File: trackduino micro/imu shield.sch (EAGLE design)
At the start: 11 parts, among them U1 LSM9DS1

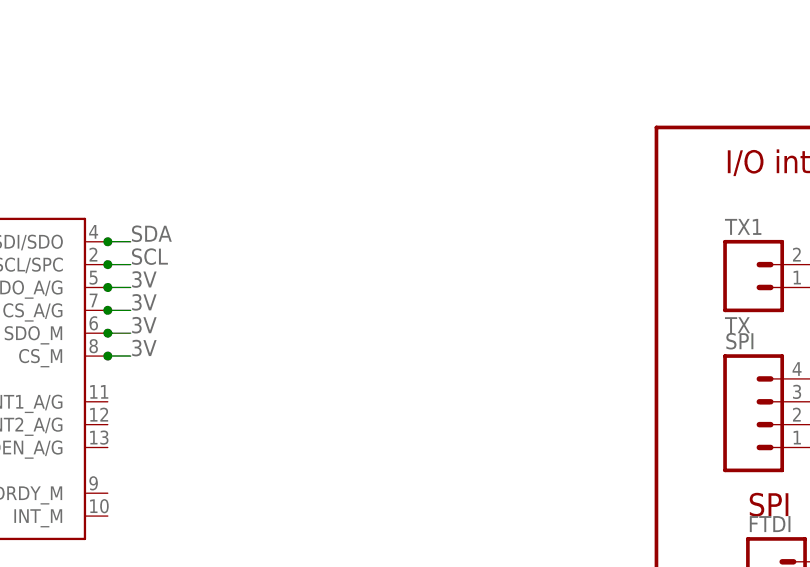
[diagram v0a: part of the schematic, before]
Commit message: added reg to imu shield
added 3v regulator to IMU shield
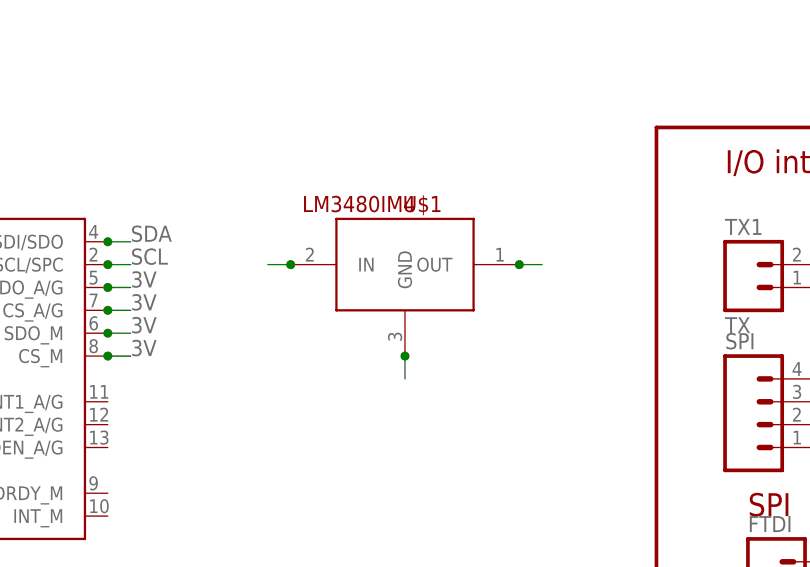
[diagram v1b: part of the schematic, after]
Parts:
- added U$1: LM3480IM4, SparkFun-PowerIC:LM3480IM4
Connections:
- net GND: now also U$1.GND
- net VCC: now also U$1.IN
- net VDD: now also U$1.OUT
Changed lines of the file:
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@@
 <part name="C4" library="SparkFun-Passives" deviceset="CAP" device="0805" value="10nf"/>
 <part name="C5" library="SparkFun-Passives" deviceset="CAP" device="0805" value=".1uf"/>
+<part name="U$1" library="SparkFun-PowerIC" deviceset="LM3480IM4" device=""/>
 </parts>
 <sheets>
@@
 <instance part="C4" gate="G$1" x="71.12" y="91.44"/>
 <instance part="C5" gate="G$1" x="78.74" y="91.44"/>
+<instance part="U$1" gate="G$1" x="154.94" y="93.98"/>
 </instances>
 <busses>
@@
 <label x="83.82" y="66.04" size="1.778" layer="95"/>
 </segment>
+<segment>
+<pinref part="U$1" gate="G$1" pin="GND"/>
+<wire x1="154.94" y1="83.82" x2="154.94" y2="81.28" width="0.1524" layer="91"/>
+<junction x="154.94" y="83.82"/>
+</segment>
 </net>
 <net name="VCC" class="0">
@@
 <junction x="203.2" y="55.88"/>
 <junction x="208.28" y="55.88"/>
+</segment>
+<segment>
+<pinref part="U$1" gate="G$1" pin="IN"/>
+<wire x1="142.24" y1="93.98" x2="139.7" y2="93.98" width="0.1524" layer="91"/>
+<junction x="142.24" y="93.98"/>
 </segment>
 </net>
@@
 <junction x="91.44" y="93.98"/>
 </segment>
-</net>
+<segment>
+<pinref part="U$1" gate="G$1" pin="OUT"/>
+<wire x1="167.64" y1="93.98" x2="170.18" y2="93.98" width="0.1524" layer="91"/>
+<junction x="167.64" y="93.98"/>
+</segment>
+</net>

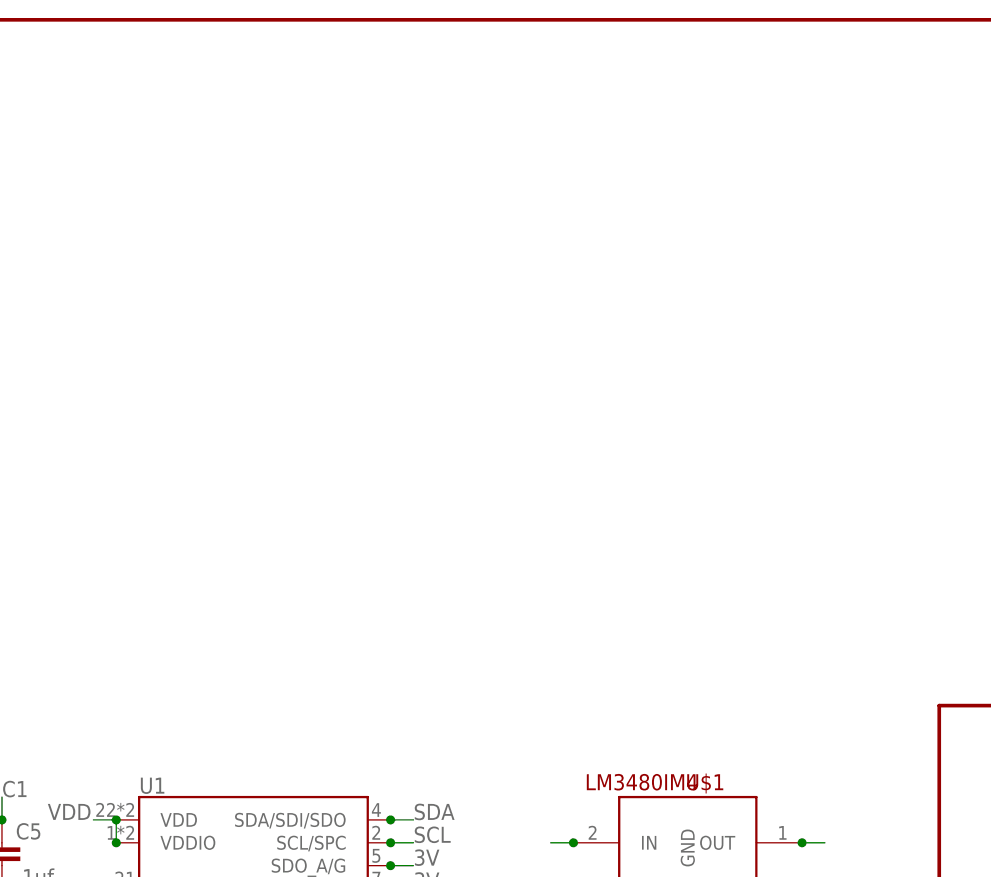
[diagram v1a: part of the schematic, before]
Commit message: Shield Updates
added sd storage shield, added fetid chip to programming shield. Moved
test boards to correct folder.
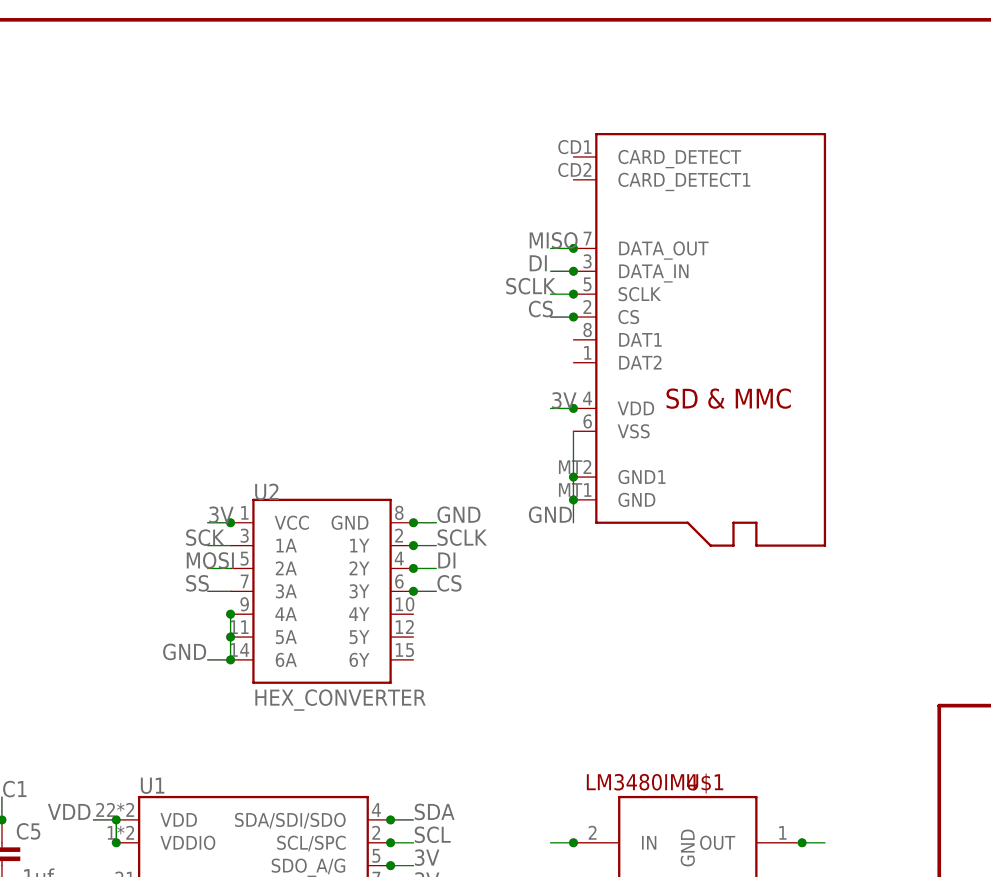
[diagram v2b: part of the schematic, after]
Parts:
- added U$2: MICROSD, adafruit:MICROSD
- added U2: HEX_CONVERTER, SparkFun-DigitalIC:HEX_CONVERTER
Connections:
- new net CS: U$2.CS, U2.3Y
- new net DI: U$2.DATA_IN, U2.2Y
- new net SCLK: U$2.SCLK, U2.1Y
- net 3V: now also U$2.VDD, U2.VCC
- net GND: now also U$2.GND, U$2.GND1, U$2.VSS, U2.4A, U2.5A, U2.6A, U2.GND
- net MISO: now also U$2.DATA_OUT
- net MOSI: now also U2.2A
- net SCK: now also U2.1A
- net SS: now also U2.3A
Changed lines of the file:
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@@
 <layer number="230" name="230bmp" color="7" fill="1" visible="yes" active="yes"/>
 <layer number="231" name="231bmp" color="7" fill="1" visible="yes" active="yes"/>
+<layer number="232" name="Eagle3D_PG2" color="7" fill="1" visible="no" active="no"/>
+<layer number="233" name="Eagle3D_PG3" color="7" fill="1" visible="no" active="no"/>
 <layer number="248" name="Housing" color="7" fill="1" visible="yes" active="yes"/>
 <layer number="249" name="Edge" color="7" fill="1" visible="yes" active="yes"/>
@@
 <part name="C5" library="SparkFun-Passives" deviceset="CAP" device="0805" value=".1uf"/>
 <part name="U$1" library="SparkFun-PowerIC" deviceset="LM3480IM4" device=""/>
+<part name="U2" library="SparkFun-DigitalIC" deviceset="HEX_CONVERTER" device=""/>
+<part name="U$2" library="adafruit" deviceset="MICROSD" device=""/>
 </parts>
 <sheets>
@@
 <instance part="C5" gate="G$1" x="78.74" y="91.44"/>
 <instance part="U$1" gate="G$1" x="154.94" y="93.98"/>
+<instance part="U2" gate="G$1" x="114.3" y="121.92"/>
+<instance part="U$2" gate="G$1" x="160.02" y="152.4"/>
 </instances>
 <busses>
@@
 <junction x="154.94" y="83.82"/>
 </segment>
+<segment>
+<pinref part="U$2" gate="G$1" pin="VSS"/>
+<wire x1="142.24" y1="139.7" x2="142.24" y2="134.62" width="0.1524" layer="91"/>
+<label x="137.16" y="129.54" size="1.778" layer="95"/>
+<pinref part="U$2" gate="G$1" pin="GND"/>
+<junction x="142.24" y="132.08"/>
+<wire x1="142.24" y1="134.62" x2="142.24" y2="132.08" width="0.1524" layer="91"/>
+<wire x1="142.24" y1="132.08" x2="142.24" y2="129.54" width="0.1524" layer="91"/>
+<pinref part="U$2" gate="G$1" pin="GND1"/>
+<junction x="142.24" y="134.62"/>
+</segment>
+<segment>
+<pinref part="U2" gate="G$1" pin="GND"/>
+<wire x1="124.46" y1="129.54" x2="127" y2="129.54" width="0.1524" layer="91"/>
+<label x="127" y="129.54" size="1.778" layer="95"/>
+<junction x="124.46" y="129.54"/>
+</segment>
+<segment>
+<pinref part="U2" gate="G$1" pin="5A"/>
+<pinref part="U2" gate="G$1" pin="6A"/>
+<wire x1="104.14" y1="116.84" x2="104.14" y2="114.3" width="0.1524" layer="91"/>
+<wire x1="104.14" y1="114.3" x2="101.6" y2="114.3" width="0.1524" layer="91"/>
+<label x="96.52" y="114.3" size="1.778" layer="95"/>
+<junction x="104.14" y="116.84"/>
+<junction x="104.14" y="114.3"/>
+<pinref part="U2" gate="G$1" pin="4A"/>
+<wire x1="104.14" y1="119.38" x2="104.14" y2="116.84" width="0.1524" layer="91"/>
+<junction x="104.14" y="119.38"/>
+</segment>
 </net>
 <net name="VCC" class="0">
@@
 <junction x="200.66" y="76.2"/>
 </segment>
+<segment>
+<pinref part="U$2" gate="G$1" pin="DATA_OUT"/>
+<wire x1="142.24" y1="160.02" x2="139.7" y2="160.02" width="0.1524" layer="91"/>
+<label x="137.16" y="160.02" size="1.778" layer="95"/>
+<junction x="142.24" y="160.02"/>
+</segment>
 </net>
 <net name="MOSI" class="0">
@@
 <junction x="200.66" y="78.74"/>
 </segment>
+<segment>
+<pinref part="U2" gate="G$1" pin="2A"/>
+<wire x1="104.14" y1="124.46" x2="101.6" y2="124.46" width="0.1524" layer="91"/>
+<label x="99.06" y="124.46" size="1.778" layer="95"/>
+</segment>
 </net>
 <net name="SCK" class="0">
@@
 <junction x="200.66" y="73.66"/>
 </segment>
+<segment>
+<pinref part="U2" gate="G$1" pin="1A"/>
+<wire x1="104.14" y1="127" x2="101.6" y2="127" width="0.1524" layer="91"/>
+<label x="99.06" y="127" size="1.778" layer="95"/>
+</segment>
 </net>
 <net name="SS" class="0">
@@
 <label x="203.2" y="81.28" size="1.778" layer="95"/>
 <junction x="200.66" y="81.28"/>
+</segment>
+<segment>
+<pinref part="U2" gate="G$1" pin="3A"/>
+<wire x1="104.14" y1="121.92" x2="101.6" y2="121.92" width="0.1524" layer="91"/>
+<label x="99.06" y="121.92" size="1.778" layer="95"/>
 </segment>
 </net>
@@
 <junction x="121.92" y="83.82"/>
 <label x="124.46" y="83.82" size="1.778" layer="95"/>
+</segment>
+<segment>
+<pinref part="U2" gate="G$1" pin="VCC"/>
+<wire x1="104.14" y1="129.54" x2="101.6" y2="129.54" width="0.1524" layer="91"/>
+<label x="101.6" y="129.54" size="1.778" layer="95"/>
+<junction x="104.14" y="129.54"/>
+</segment>
+<segment>
+<pinref part="U$2" gate="G$1" pin="VDD"/>
+<wire x1="142.24" y1="142.24" x2="139.7" y2="142.24" width="0.1524" layer="91"/>
+<label x="139.7" y="142.24" size="1.778" layer="95"/>
+<junction x="142.24" y="142.24"/>
 </segment>
 </net>
@@
 </segment>
 </net>
+<net name="DI" class="0">
+<segment>
+<pinref part="U$2" gate="G$1" pin="DATA_IN"/>
+<wire x1="142.24" y1="157.48" x2="139.7" y2="157.48" width="0.1524" layer="91"/>
+<label x="137.16" y="157.48" size="1.778" layer="95"/>
+<junction x="142.24" y="157.48"/>
+</segment>
+<segment>
+<pinref part="U2" gate="G$1" pin="2Y"/>
+<wire x1="124.46" y1="124.46" x2="127" y2="124.46" width="0.1524" layer="91"/>
+<label x="127" y="124.46" size="1.778" layer="95"/>
+<junction x="124.46" y="124.46"/>
+</segment>
+</net>
+<net name="SCLK" class="0">
+<segment>
+<pinref part="U$2" gate="G$1" pin="SCLK"/>
+<wire x1="142.24" y1="154.94" x2="139.7" y2="154.94" width="0.1524" layer="91"/>
+<label x="134.62" y="154.94" size="1.778" layer="95"/>
+<junction x="142.24" y="154.94"/>
+</segment>
+<segment>
+<pinref part="U2" gate="G$1" pin="1Y"/>
+<wire x1="124.46" y1="127" x2="127" y2="127" width="0.1524" layer="91"/>
+<label x="127" y="127" size="1.778" layer="95"/>
+<junction x="124.46" y="127"/>
+</segment>
+</net>
+<net name="CS" class="0">
+<segment>
+<pinref part="U$2" gate="G$1" pin="CS"/>
+<wire x1="142.24" y1="152.4" x2="139.7" y2="152.4" width="0.1524" layer="91"/>
+<label x="137.16" y="152.4" size="1.778" layer="95"/>
+<junction x="142.24" y="152.4"/>
+</segment>
+<segment>
+<pinref part="U2" gate="G$1" pin="3Y"/>
+<wire x1="124.46" y1="121.92" x2="127" y2="121.92" width="0.1524" layer="91"/>
+<label x="127" y="121.92" size="1.778" layer="95"/>
+<junction x="124.46" y="121.92"/>
+</segment>
+</net>
